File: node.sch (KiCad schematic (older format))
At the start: 0 parts

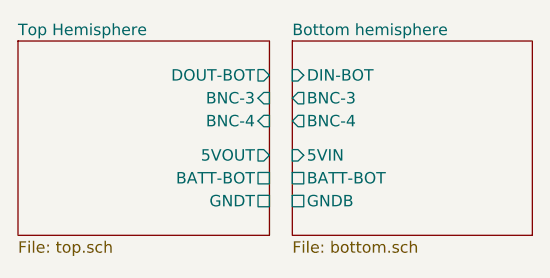
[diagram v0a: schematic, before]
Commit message: Rename nets, fix ERC warnings and errors
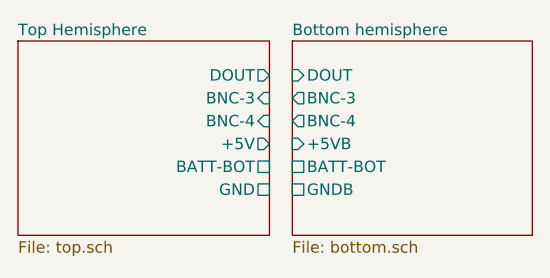
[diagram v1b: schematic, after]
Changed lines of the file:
@@
 F0 "Top Hemisphere" 50
 F1 "top.sch" 50
-F2 "GNDT" U R 5550 3750 50
-F3 "BATT-BOT" U R 5550 3650 50
+F2 "GND" U R 5550 3700 50
+F3 "BATT-BOT" U R 5550 3600 50
 F4 "BNC-3" I R 5550 3300 50
 F5 "BNC-4" I R 5550 3400 50
-F6 "DOUT-BOT" O R 5550 3200 50
-F7 "5VOUT" O R 5550 3550 50
+F6 "DOUT" O R 5550 3200 50
+F7 "+5V" O R 5550 3500 50
 $EndSheet
 $Sheet
@@
 F0 "Bottom hemisphere" 50
 F1 "bottom.sch" 50
-F2 "5VIN" I L 5650 3550 50
-F3 "BATT-BOT" U L 5650 3650 50
-F4 "GNDB" U L 5650 3750 50
+F2 "+5VB" I L 5650 3500 50
+F3 "BATT-BOT" U L 5650 3600 50
+F4 "GNDB" U L 5650 3700 50
 F5 "BNC-3" O L 5650 3300 50
 F6 "BNC-4" O L 5650 3400 50
-F7 "DIN-BOT" I L 5650 3200 50
+F7 "DOUT" I L 5650 3200 50
 $EndSheet
 $EndSCHEMATC
